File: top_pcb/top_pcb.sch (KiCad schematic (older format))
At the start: 4 parts, among them J1 flat_cable_connector, J2 header, J3 free_holes, J4 Conn_01x04

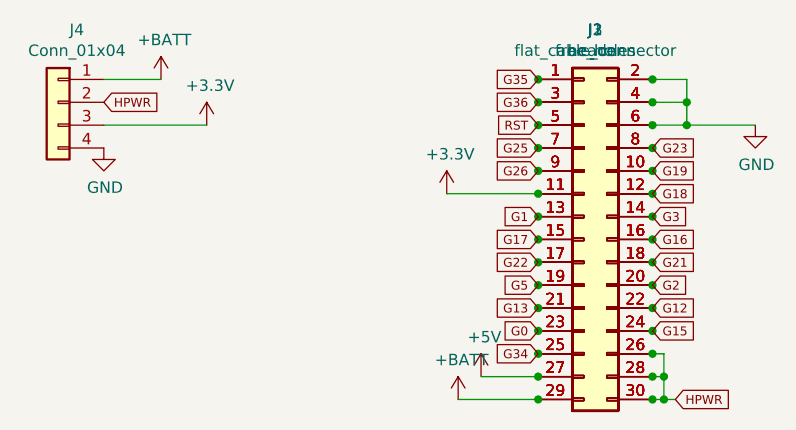
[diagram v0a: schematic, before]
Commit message: Separate HPWR to NC0-2 for Core2
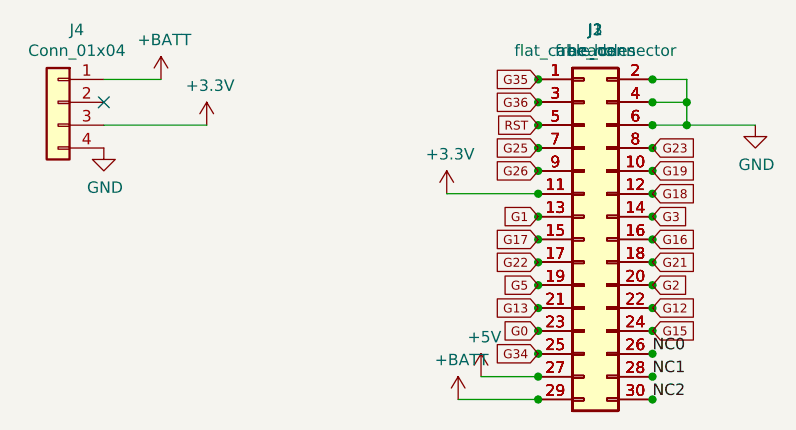
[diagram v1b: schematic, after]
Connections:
- removed net HPWR: J1.26 (Pin_26), J1.28 (Pin_28), J1.30 (Pin_30), J2.26 (Pin_26), J2.28 (Pin_28), J2.30 (Pin_30), J3.26 (Pin_26), J3.28 (Pin_28), J3.30 (Pin_30), J4.2 (Pin_2)
- new net NC0: J1.26 (Pin_26), J2.26 (Pin_26), J3.26 (Pin_26)
- new net NC1: J1.28 (Pin_28), J2.28 (Pin_28), J3.28 (Pin_28)
- new net NC2: J1.30 (Pin_30), J2.30 (Pin_30), J3.30 (Pin_30)
- no-connect marks 0 -> 1
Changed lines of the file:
@@
 Text GLabel 8400 3100 2    39   Input ~ 0
 G15
-Text GLabel 8500 3400 2    39   Input ~ 0
-HPWR
-Wire Wire Line
-	8400 3400 8450 3400
-Wire Wire Line
-	8450 3400 8450 3300
-Wire Wire Line
-	8450 3200 8400 3200
-Connection ~ 8450 3400
-Wire Wire Line
-	8450 3400 8500 3400
-Wire Wire Line
-	8400 3300 8450 3300
-Connection ~ 8450 3300
-Wire Wire Line
-	8450 3300 8450 3200
 $Comp
 L power:GND #PWR0109
@@
 Wire Wire Line
 	7900 2500 7500 2500
-Connection ~ 8400 3400
 Connection ~ 7900 3400
 Connection ~ 7900 2500
@@
 Connection ~ 8400 2100
 Connection ~ 8400 2000
-Connection ~ 8400 3300
 Connection ~ 7900 3300
-Connection ~ 8400 3200
 $Comp
 L Connector_Generic:Conn_02x15_Odd_Even J3
@@
 	-1   0    0    -1
 $EndComp
-Text GLabel 6000 2100 2    39   Input ~ 0
-HPWR
 $Comp
 L power:GND #PWR0101
@@
 Wire Wire Line
 	6000 2200 6450 2200
+NoConn ~ 6000 2100
+Text Label 8400 3200 0    50   ~ 0
+NC0
+Connection ~ 8400 3200
+Text Label 8400 3300 0    50   ~ 0
+NC1
+Connection ~ 8400 3300
+Text Label 8400 3400 0    50   ~ 0
+NC2
+Connection ~ 8400 3400
 $EndSCHEMATC
